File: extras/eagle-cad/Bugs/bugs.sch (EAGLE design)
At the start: 19 parts, among them M1 WIREPADSMD5-2,5, M2 WIREPADSMD5-2,5, M3 WIREPADSMD5-2,5, M4 WIREPADSMD5-2,5

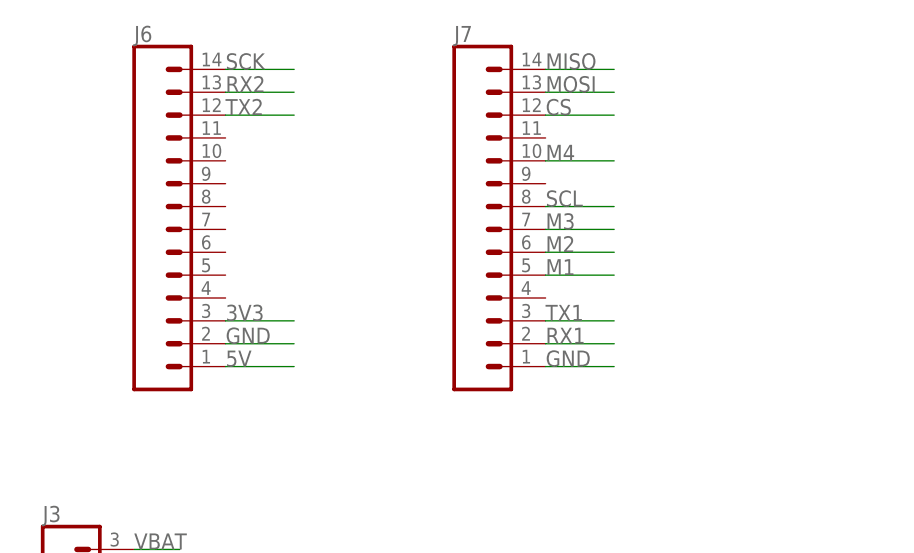
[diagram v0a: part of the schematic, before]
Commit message: Restored Bugs board
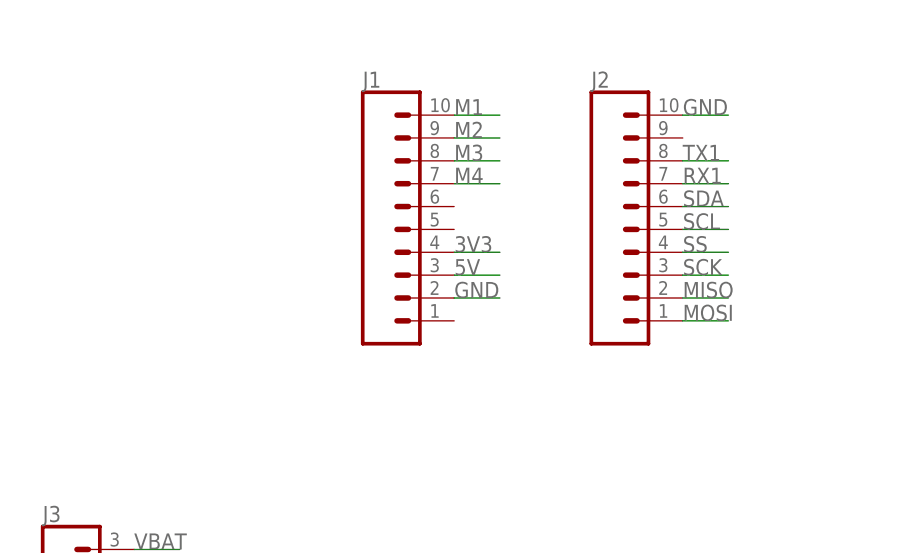
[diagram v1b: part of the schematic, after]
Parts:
- removed J6, J7: (no value), SparkFun-Connectors:CONN_14NO_SILK
- added J1, J2: (no value), SparkFun-Connectors:CONN_10NO_SILK_PTH_FEMALE
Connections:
- removed net CS: J7.12
- removed net RX2: J6.13
- removed net TX2: J6.12
- new net SS: J2.4
- net 3V3: now also J1.4; no longer J6.3
- net 5V: now also J1.3; no longer J6.1
- net GND: now also J1.2, J2.10; no longer J6.2, J7.1
- net M1: now also J1.10; no longer J7.5
- net M2: now also J1.9; no longer J7.6
- net M3: now also J1.8; no longer J7.7
- net M4: now also J1.7; no longer J7.10
- net MISO: now also J2.2; no longer J7.14
- net MOSI: now also J2.1; no longer J7.13
- net RX1: now also J2.7; no longer J7.2
- net SCK: now also J2.3; no longer J6.14
- net SCL: now also J2.5; no longer J7.8
- net SDA: now also J2.6
- net TX1: now also J2.8; no longer J7.3
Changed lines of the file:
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@@
 <part name="GND" library="wirepad" deviceset="WIREPAD" device="SMD5-2,5"/>
 <part name="VBAT" library="wirepad" deviceset="WIREPAD" device="SMD5-2,5"/>
+<part name="J1" library="SparkFun-Connectors" deviceset="CONN_10" device="NO_SILK_PTH_FEMALE"/>
+<part name="J2" library="SparkFun-Connectors" deviceset="CONN_10" device="NO_SILK_PTH_FEMALE"/>
 <part name="J3" library="SparkFun-Connectors" deviceset="CONN_03" device="1X03_NO_SILK"/>
 <part name="J4" library="SparkFun-Connectors" deviceset="CONN_05" device="NO_SILK"/>
@@
 <part name="VBAT4" library="wirepad" deviceset="WIREPAD" device="SMD5-2,5"/>
 <part name="J5" library="SparkFun-Connectors" deviceset="CONN_03" device="1X03_NO_SILK"/>
-<part name="J6" library="SparkFun-Connectors" deviceset="CONN_14" device="NO_SILK"/>
-<part name="J7" library="SparkFun-Connectors" deviceset="CONN_14" device="NO_SILK"/>
 </parts>
 <sheets>
@@
 </instance>
 <instance part="VBAT" gate="G$1" x="2.54" y="-12.7" smashed="yes"/>
+<instance part="J1" gate="J1" x="-15.24" y="68.58" smashed="yes">
+<attribute name="VALUE" x="-15.24" y="45.974" size="1.778" layer="96" font="vector"/>
+<attribute name="NAME" x="-15.24" y="76.708" size="1.778" layer="95" font="vector"/>
+</instance>
+<instance part="J2" gate="J1" x="10.16" y="68.58" smashed="yes">
+<attribute name="VALUE" x="10.16" y="45.974" size="1.778" layer="96" font="vector"/>
+<attribute name="NAME" x="10.16" y="76.708" size="1.778" layer="95" font="vector"/>
+</instance>
 <instance part="J3" gate="J$1" x="-48.26" y="22.86" smashed="yes">
 <attribute name="VALUE" x="-50.8" y="15.494" size="1.778" layer="96" font="vector"/>
@@
 <attribute name="VALUE" x="-38.1" y="-42.926" size="1.778" layer="96" font="vector"/>
 </instance>
-<instance part="J6" gate="G$1" x="-40.64" y="63.5"/>
-<instance part="J7" gate="G$1" x="-5.08" y="63.5"/>
 </instances>
 <busses>
@@
 <net name="GND" class="0">
 <segment>
+<pinref part="J1" gate="J1" pin="2"/>
+<wire x1="-5.08" y1="53.34" x2="0" y2="53.34" width="0.1524" layer="91"/>
+<label x="-5.08" y="53.34" size="1.778" layer="95"/>
+</segment>
+<segment>
+<pinref part="J2" gate="J1" pin="10"/>
+<wire x1="20.32" y1="73.66" x2="25.4" y2="73.66" width="0.1524" layer="91"/>
+<label x="20.32" y="73.66" size="1.778" layer="95"/>
+</segment>
+<segment>
 <pinref part="J3" gate="J$1" pin="2"/>
 <wire x1="-40.64" y1="22.86" x2="-35.56" y2="22.86" width="0.1524" layer="91"/>
@@
 <label x="-27.94" y="-35.56" size="1.778" layer="95"/>
 </segment>
-<segment>
-<pinref part="J6" gate="G$1" pin="2"/>
-<wire x1="-30.48" y1="48.26" x2="-22.86" y2="48.26" width="0.1524" layer="91"/>
-<label x="-30.48" y="48.26" size="1.778" layer="95"/>
-</segment>
-<segment>
-<pinref part="J7" gate="G$1" pin="1"/>
-<wire x1="5.08" y1="45.72" x2="12.7" y2="45.72" width="0.1524" layer="91"/>
-<label x="5.08" y="45.72" size="1.778" layer="95"/>
-</segment>
 </net>
 <net name="5V" class="0">
+<segment>
+<pinref part="J1" gate="J1" pin="3"/>
+<wire x1="-5.08" y1="55.88" x2="0" y2="55.88" width="0.1524" layer="91"/>
+<label x="-5.08" y="55.88" size="1.778" layer="95"/>
+</segment>
 <segment>
 <pinref part="J3" gate="J$1" pin="1"/>
@@
 <label x="-27.94" y="-38.1" size="1.778" layer="95"/>
 </segment>
-<segment>
-<pinref part="J6" gate="G$1" pin="1"/>
-<wire x1="-30.48" y1="45.72" x2="-22.86" y2="45.72" width="0.1524" layer="91"/>
-<label x="-30.48" y="45.72" size="1.778" layer="95"/>
-</segment>
 </net>
 <net name="3V3" class="0">
+<segment>
+<pinref part="J1" gate="J1" pin="4"/>
+<wire x1="-5.08" y1="58.42" x2="0" y2="58.42" width="0.1524" layer="91"/>
+<label x="-5.08" y="58.42" size="1.778" layer="95"/>
+</segment>
 <segment>
 <pinref part="J4" gate="G$1" pin="4"/>
@@
 <label x="-43.18" y="-5.08" size="1.778" layer="95"/>
 </segment>
-<segment>
-<pinref part="J6" gate="G$1" pin="3"/>
-<wire x1="-30.48" y1="50.8" x2="-22.86" y2="50.8" width="0.1524" layer="91"/>
-<label x="-30.48" y="50.8" size="1.778" layer="95"/>
-</segment>
 </net>
 <net name="M1" class="0">
+<segment>
+<pinref part="J1" gate="J1" pin="10"/>
+<wire x1="-5.08" y1="73.66" x2="0" y2="73.66" width="0.1524" layer="91"/>
+<label x="-5.08" y="73.66" size="1.778" layer="95"/>
+</segment>
 <segment>
 <pinref part="M1" gate="G$1" pin="P"/>
@@
 <label x="7.62" y="-66.04" size="1.778" layer="95"/>
 </segment>
-<segment>
-<pinref part="J7" gate="G$1" pin="5"/>
-<wire x1="5.08" y1="55.88" x2="12.7" y2="55.88" width="0.1524" layer="91"/>
-<label x="5.08" y="55.88" size="1.778" layer="95"/>
-</segment>
 </net>
 <net name="M2" class="0">
+<segment>
+<pinref part="J1" gate="J1" pin="9"/>
+<wire x1="-5.08" y1="71.12" x2="0" y2="71.12" width="0.1524" layer="91"/>
+<label x="-5.08" y="71.12" size="1.778" layer="95"/>
+</segment>
 <segment>
 <pinref part="M2" gate="G$1" pin="P"/>
@@
 <label x="68.58" y="-20.32" size="1.778" layer="95"/>
 </segment>
-<segment>
-<pinref part="J7" gate="G$1" pin="6"/>
-<wire x1="5.08" y1="58.42" x2="12.7" y2="58.42" width="0.1524" layer="91"/>
-<label x="5.08" y="58.42" size="1.778" layer="95"/>
-</segment>
 </net>
 <net name="M3" class="0">
+<segment>
+<pinref part="J1" gate="J1" pin="8"/>
+<wire x1="-5.08" y1="68.58" x2="0" y2="68.58" width="0.1524" layer="91"/>
+<label x="-5.08" y="68.58" size="1.778" layer="95"/>
+</segment>
 <segment>
 <pinref part="M3" gate="G$1" pin="P"/>
@@
 <label x="71.12" y="-66.04" size="1.778" layer="95"/>
 </segment>
-<segment>
-<pinref part="J7" gate="G$1" pin="7"/>
-<wire x1="5.08" y1="60.96" x2="12.7" y2="60.96" width="0.1524" layer="91"/>
-<label x="5.08" y="60.96" size="1.778" layer="95"/>
-</segment>
 </net>
 <net name="M4" class="0">
+<segment>
+<pinref part="J1" gate="J1" pin="7"/>
+<wire x1="-5.08" y1="66.04" x2="0" y2="66.04" width="0.1524" layer="91"/>
+<label x="-5.08" y="66.04" size="1.778" layer="95"/>
+</segment>
 <segment>
 <pinref part="M4" gate="G$1" pin="P"/>
@@
 <label x="5.08" y="-22.86" size="1.778" layer="95"/>
 </segment>
-<segment>
-<pinref part="J7" gate="G$1" pin="10"/>
-<wire x1="5.08" y1="68.58" x2="12.7" y2="68.58" width="0.1524" layer="91"/>
-<label x="5.08" y="68.58" size="1.778" layer="95"/>
-</segment>
 </net>
 <net name="SCL" class="0">
@@
 </segment>
 <segment>
-<pinref part="J7" gate="G$1" pin="8"/>
-<wire x1="5.08" y1="63.5" x2="12.7" y2="63.5" width="0.1524" layer="91"/>
-<label x="5.08" y="63.5" size="1.778" layer="95"/>
+<pinref part="J2" gate="J1" pin="5"/>
+<wire x1="20.32" y1="60.96" x2="25.4" y2="60.96" width="0.1524" layer="91"/>
+<label x="20.32" y="60.96" size="1.778" layer="95"/>
 </segment>
 </net>
@@
 <label x="-43.18" y="-12.7" size="1.778" layer="95"/>
 </segment>
+<segment>
+<pinref part="J2" gate="J1" pin="6"/>
+<wire x1="20.32" y1="63.5" x2="25.4" y2="63.5" width="0.1524" layer="91"/>
+<label x="20.32" y="63.5" size="1.778" layer="95"/>
+</segment>
+</net>
+<net name="SS" class="0">
+<segment>
+<pinref part="J2" gate="J1" pin="4"/>
+<wire x1="20.32" y1="58.42" x2="25.4" y2="58.42" width="0.1524" layer="91"/>
+<label x="20.32" y="58.42" size="1.778" layer="95"/>
+</segment>
 </net>
 <net name="SCK" class="0">
 <segment>
-<pinref part="J6" gate="G$1" pin="14"/>
-<wire x1="-30.48" y1="78.74" x2="-22.86" y2="78.74" width="0.1524" layer="91"/>
-<label x="-30.48" y="78.74" size="1.778" layer="95"/>
+<pinref part="J2" gate="J1" pin="3"/>
+<wire x1="20.32" y1="55.88" x2="25.4" y2="55.88" width="0.1524" layer="91"/>
+<label x="20.32" y="55.88" size="1.778" layer="95"/>
 </segment>
 </net>
 <net name="MISO" class="0">
 <segment>
-<pinref part="J7" gate="G$1" pin="14"/>
-<wire x1="5.08" y1="78.74" x2="12.7" y2="78.74" width="0.1524" layer="91"/>
-<label x="5.08" y="78.74" size="1.778" layer="95"/>
+<pinref part="J2" gate="J1" pin="2"/>
+<wire x1="20.32" y1="53.34" x2="25.4" y2="53.34" width="0.1524" layer="91"/>
+<label x="20.32" y="53.34" size="1.778" layer="95"/>
 </segment>
 </net>
 <net name="MOSI" class="0">
 <segment>
-<pinref part="J7" gate="G$1" pin="13"/>
-<wire x1="5.08" y1="76.2" x2="12.7" y2="76.2" width="0.1524" layer="91"/>
-<label x="5.08" y="76.2" size="1.778" layer="95"/>
+<pinref part="J2" gate="J1" pin="1"/>
+<wire x1="20.32" y1="50.8" x2="25.4" y2="50.8" width="0.1524" layer="91"/>
+<label x="20.32" y="50.8" size="1.778" layer="95"/>
 </segment>
 </net>
@@
 </segment>
 <segment>
-<pinref part="J7" gate="G$1" pin="2"/>
-<wire x1="5.08" y1="48.26" x2="12.7" y2="48.26" width="0.1524" layer="91"/>
-<label x="5.08" y="48.26" size="1.778" layer="95"/>
+<pinref part="J2" gate="J1" pin="7"/>
+<wire x1="20.32" y1="66.04" x2="25.4" y2="66.04" width="0.1524" layer="91"/>
+<label x="20.32" y="66.04" size="1.778" layer="95"/>
 </segment>
 </net>
@@
 <net name="TX1" class="0">
 <segment>
-<pinref part="J7" gate="G$1" pin="3"/>
-<wire x1="5.08" y1="50.8" x2="12.7" y2="50.8" width="0.1524" layer="91"/>
-<label x="5.08" y="50.8" size="1.778" layer="95"/>
-</segment>
-</net>
-<net name="RX2" class="0">
-<segment>
-<pinref part="J6" gate="G$1" pin="13"/>
-<wire x1="-30.48" y1="76.2" x2="-22.86" y2="76.2" width="0.1524" layer="91"/>
-<label x="-30.48" y="76.2" size="1.778" layer="95"/>
-</segment>
-</net>
-<net name="TX2" class="0">
-<segment>
-<pinref part="J6" gate="G$1" pin="12"/>
-<wire x1="-30.48" y1="73.66" x2="-22.86" y2="73.66" width="0.1524" layer="91"/>
-<label x="-30.48" y="73.66" size="1.778" layer="95"/>
-</segment>
-</net>
-<net name="CS" class="0">
-<segment>
-<pinref part="J7" gate="G$1" pin="12"/>
-<wire x1="5.08" y1="73.66" x2="12.7" y2="73.66" width="0.1524" layer="91"/>
-<label x="5.08" y="73.66" size="1.778" layer="95"/>
-</segment>
-</net>
+<pinref part="J2" gate="J1" pin="8"/>
+<wire x1="20.32" y1="68.58" x2="25.4" y2="68.58" width="0.1524" layer="91"/>
+<label x="20.32" y="68.58" size="1.778" layer="95"/>
+</segment>
+</net>
